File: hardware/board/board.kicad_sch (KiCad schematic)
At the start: 38 parts, among them J1 DC THRU, J2 DC THRU, J3 DC OUT, J4 DC IN, J5 DC IN, J6 DC OUT, J7 Eurorack Power, J8 Eurorack Power, SW1 ON/OFF, U1 VX7805-500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

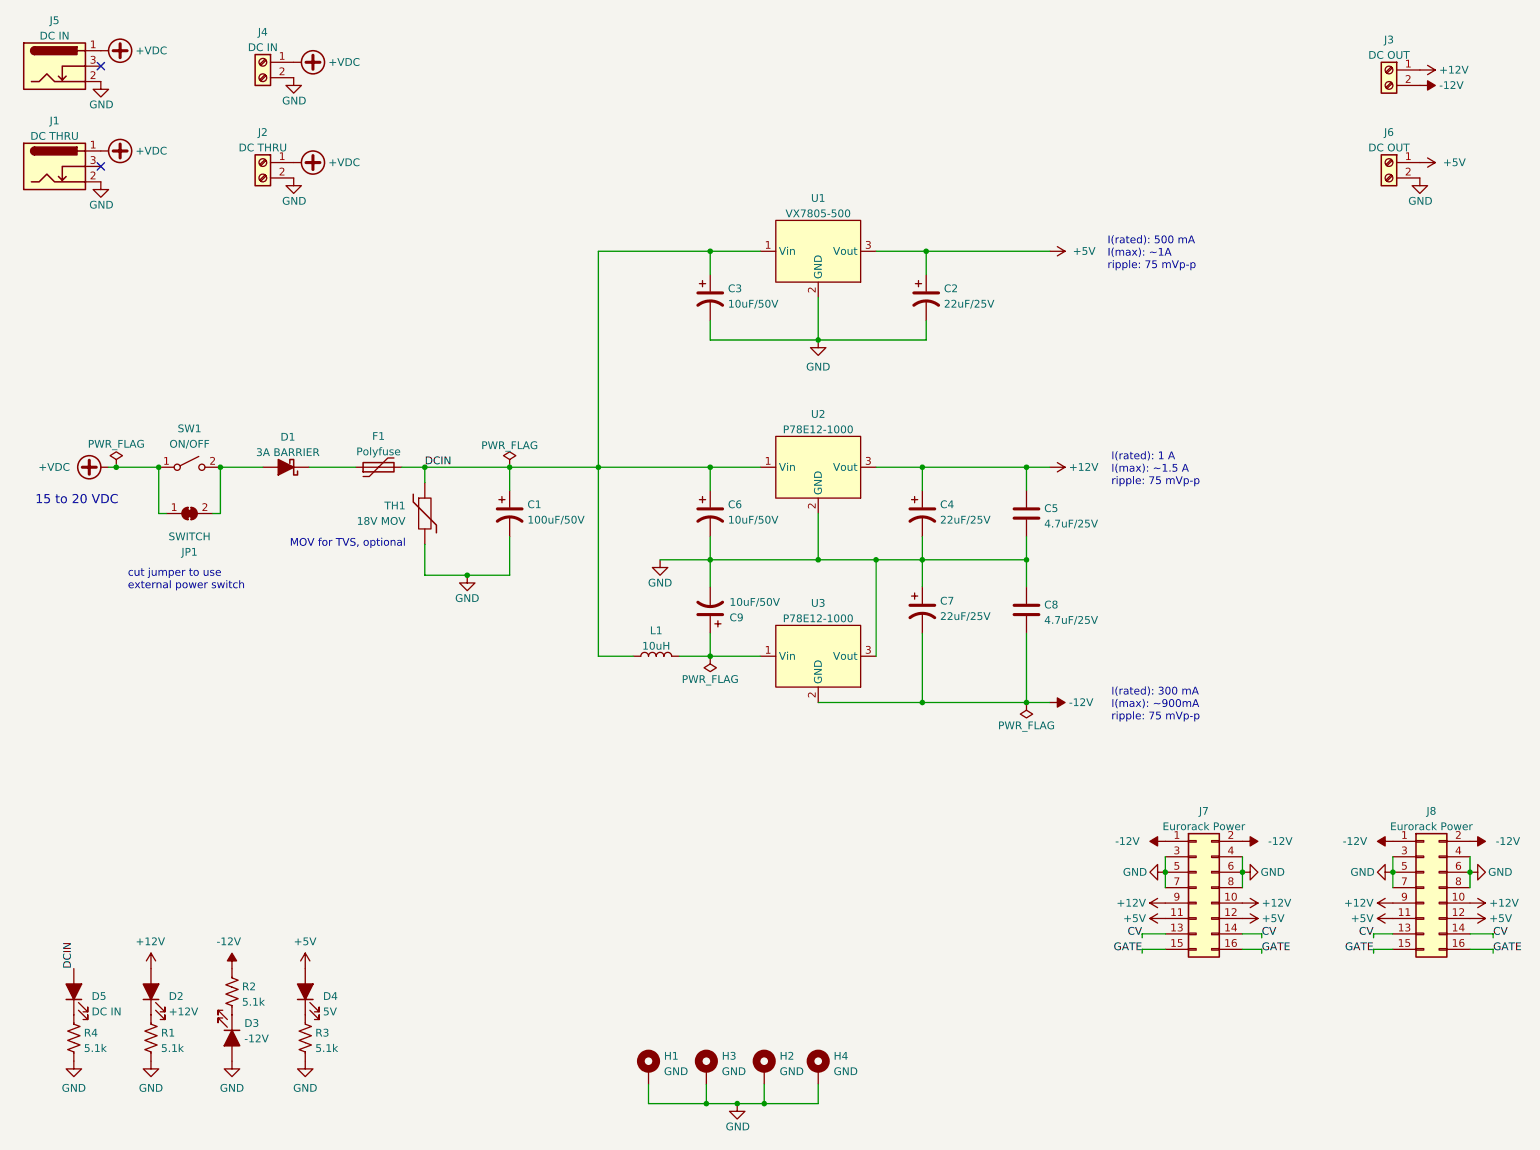
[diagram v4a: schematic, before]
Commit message: Update schematic with new name and organize it a little
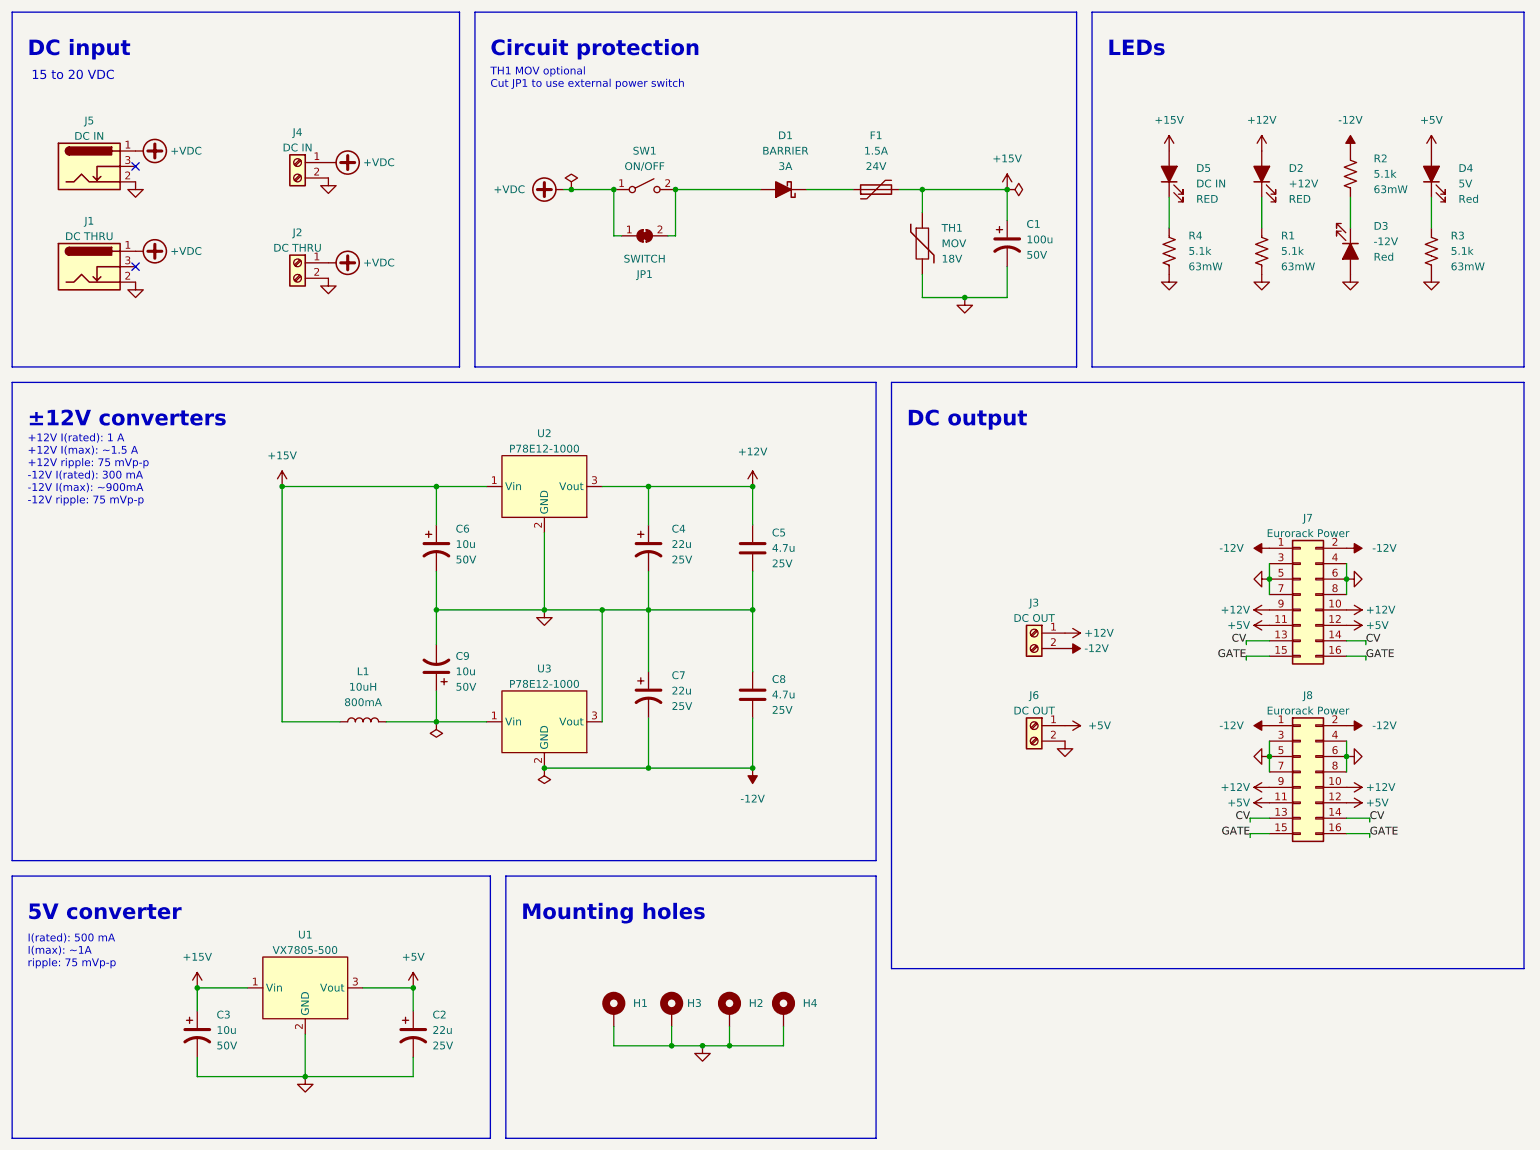
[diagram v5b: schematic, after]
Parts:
- C1: value 100uF/50V -> 100u; Rating (none) -> 50V
- C2, C4: value 22uF/25V -> 22u; Rating (none) -> 25V
- C3, C6, C9: value 10uF/50V -> 10u; Rating (none) -> 50V
- C5, C8: value 4.7uF/25V -> 4.7u; Rating (none) -> 25V
- C7: value 22uF/25V -> 22u; Field4 (none) -> 25V
- D1: value 3A BARRIER -> BARRIER; Rating (none) -> 3A
- D2, D5: Color (none) -> RED
- D3, D4: Color (none) -> Red
- F1: value Polyfuse -> 1.5A; Rating (none) -> 24V
- L1: Rating (none) -> 800mA
- R1, R2, R3, R4: Rating (none) -> 63mW
- TH1: value 18V MOV -> MOV; Rating (none) -> 18V
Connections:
- net DCIN renamed +15V
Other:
- note added: "+12V I(rated): 1 A +12V I(max): ~1.5 A +12V ripple: 75 mVp-p -12V I(rated): 300 mA -12V I(max): ~900mA -12V ripple: 75 mVp-p"
- note added: "5V converter"
- note added: "Circuit protection"
- note added: "DC input"
- note added: "DC output"
- note added: "LEDs"
- note added: "Mounting holes"
- note added: "TH1 MOV optional Cut JP1 to use external power switch"
- note added: "±12V converters"
- note removed: "I(rated): 1 A I(max): ~1.5 A ripple: 75 mVp-p"
- note removed: "I(rated): 300 mA I(max): ~900mA ripple: 75 mVp-p"
- note removed: "MOV for TVS, optional"
- note removed: "cut jumper to use external power switch"
- title: Nickel -> Micronova
- moved on the sheet: C1, C2, C3, C4, C5, C6, C7, C8, C9, D1, D2, D3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

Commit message: hardware: various updates (v4)
- switched to winterbloom footprints for caps and resistors
- use fancytext labels
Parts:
- C2, C4, C5, C7, C8: footprint Capacitor_SMD:C_0805_2012Metric_Pad1.18x1.45mm_HandSolder -> winterbloom:C_0805_HandSolder
- C3, C6, C9: footprint Capacitor_SMD:C_1206_3216Metric_Pad1.33x1.80mm_HandSolder -> winterbloom:C_1206_HandSolder
- R1, R2, R3, R4: footprint Resistor_SMD:R_0603_1608Metric_Pad0.98x0.95mm_HandSolder -> winterbloom:R_0603_HandSolder
- TH1: footprint Resistor_SMD:R_0805_2012Metric_Pad1.20x1.40mm_HandSolder -> winterbloom:R_0805_HandSolder

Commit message: Fixup some MPNs
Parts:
- C7: Field4 25V -> (none); Rating (none) -> 25V
- D2: Color RED -> (none); Rating (none) -> Red
- D3, D4: Color Red -> (none); Rating (none) -> Red
- D5: value DC IN -> DCIN; Color RED -> (none); Rating (none) -> Red
- J1: mpn PJ202-A -> PJ-102A
- J2, J4: mpn (none) -> 20020327-C021B01LF
- J3, J6: mpn 20020327-C021B01LF -> 20020327-C021B01LF
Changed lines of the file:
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@@
       (effects (font (size 1.27 1.27)) hide)
     )
-    (property "Color" "Red" (id 5) (at 239.395 55.5624 90)
-      (effects (font (size 1.27 1.27)) (justify left))
+    (property "Color" "" (id 5) (at 239.395 55.5624 90)
+      (effects (font (size 1.27 1.27)) (justify left))
+    )
+    (property "Rating" "Red" (id 6) (at 235.585 54.61 0)
+      (effects (font (size 1.27 1.27)) hide)
     )
     (pin "1")
@@
       (effects (font (size 1.27 1.27)) hide)
     )
-    (property "Color" "Red" (id 5) (at 253.365 46.0374 90)
+    (property "Color" "" (id 5) (at 253.365 46.0374 90)
       (effects (font (size 1.27 1.27)) (justify right))
+    )
+    (property "Rating" "Red" (id 6) (at 248.92 41.91 0)
+      (effects (font (size 1.27 1.27)) hide)
     )
     (pin "1")
@@
       (effects (font (size 1.27 1.27)) hide)
     )
-    (property "Field4" "25V" (id 4) (at 123.825 129.5399 0)
-      (effects (font (size 1.27 1.27)) (justify left))
+    (property "Field4" "" (id 4) (at 123.825 129.5399 0)
+      (effects (font (size 1.27 1.27)) (justify left))
+    )
+    (property "Rating" "25V" (id 5) (at 120.015 127.635 0)
+      (effects (font (size 1.27 1.27)) hide)
     )
     (pin "1")
@@
       (effects (font (size 1.27 1.27)) hide)
     )
-    (property "mpn" " 20020327-C021B01LF" (id 4) (at 183.515 132.715 0)
+    (property "mpn" "20020327-C021B01LF" (id 4) (at 183.515 132.715 0)
       (effects (font (size 1.27 1.27)) hide)
     )
@@
       (effects (font (size 1.27 1.27)) (justify right))
     )
-    (property "Value" "DC IN" (id 1) (at 210.185 43.4974 90)
+    (property "Value" "DCIN" (id 1) (at 210.185 43.4974 90)
       (effects (font (size 1.27 1.27)) (justify right))
     )
@@
       (effects (font (size 1.27 1.27)) hide)
     )
-    (property "Color" "RED" (id 5) (at 210.185 46.0374 90)
+    (property "Color" "" (id 5) (at 210.185 46.0374 90)
       (effects (font (size 1.27 1.27)) (justify right))
+    )
+    (property "Rating" "Red" (id 6) (at 205.74 41.91 0)
+      (effects (font (size 1.27 1.27)) hide)
     )
     (pin "1")
@@
       (effects (font (size 1.27 1.27)) hide)
     )
-    (property "Color" "RED" (id 5) (at 225.425 46.0374 90)
+    (property "Color" "" (id 5) (at 225.425 46.0374 90)
       (effects (font (size 1.27 1.27)) (justify right))
+    )
+    (property "Rating" "Red" (id 6) (at 220.98 41.91 0)
+      (effects (font (size 1.27 1.27)) hide)
     )
     (pin "1")
@@
       (effects (font (size 1.27 1.27)) hide)
     )
+    (property "mpn" "20020327-C021B01LF" (id 4) (at 62.23 40.005 0)
+      (effects (font (size 1.27 1.27)) hide)
+    )
     (pin "1")
     (pin "2")
@@
       (effects (font (size 1.27 1.27)) hide)
     )
-    (property "mpn" " 20020327-C021B01LF" (id 4) (at 183.515 117.475 0)
+    (property "mpn" "20020327-C021B01LF" (id 4) (at 183.515 117.475 0)
       (effects (font (size 1.27 1.27)) hide)
     )
@@
       (effects (font (size 1.27 1.27)) hide)
     )
+    (property "mpn" "20020327-C021B01LF" (id 4) (at 62.23 56.515 0)
+      (effects (font (size 1.27 1.27)) hide)
+    )
     (pin "1")
     (pin "2")
@@
       (effects (font (size 1.27 1.27)) hide)
     )
-    (property "mpn" "PJ202-A" (id 4) (at 27.94 57.15 0)
+    (property "mpn" "PJ-102A" (id 4) (at 27.94 57.15 0)
       (effects (font (size 1.27 1.27)) hide)
     )
@@
     )
     (path "/34740818-b789-4604-a20b-8e132e8ced54"
-      (reference "D5") (unit 1) (value "DC IN") (footprint "winterbloom:LED_0805_Kingbright_APT2012")
+      (reference "D5") (unit 1) (value "DCIN") (footprint "winterbloom:LED_0805_Kingbright_APT2012")
     )
     (path "/6b28564a-fc8d-47f4-a7ed-28e20f1c054c"
